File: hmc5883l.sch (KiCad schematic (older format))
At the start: 6 parts, among them U5 HMC5883L

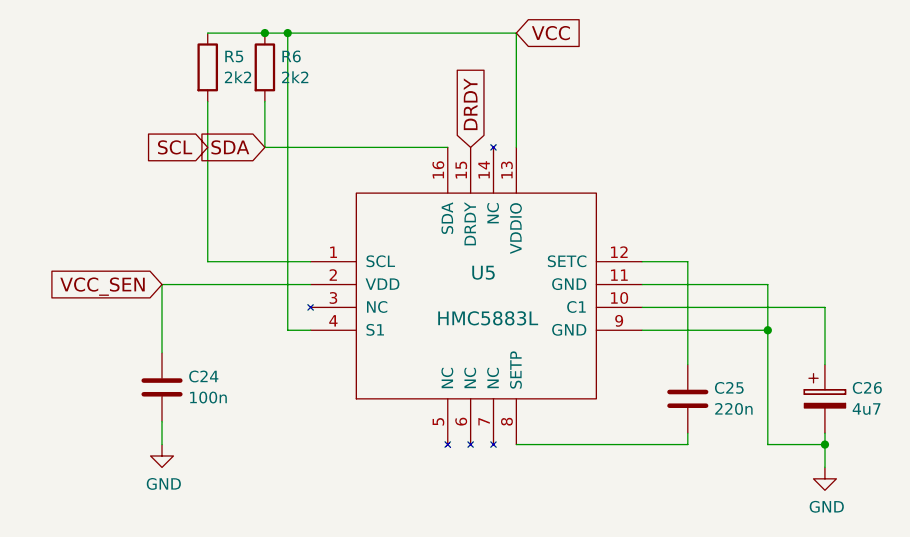
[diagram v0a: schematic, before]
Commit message: changed some netnames
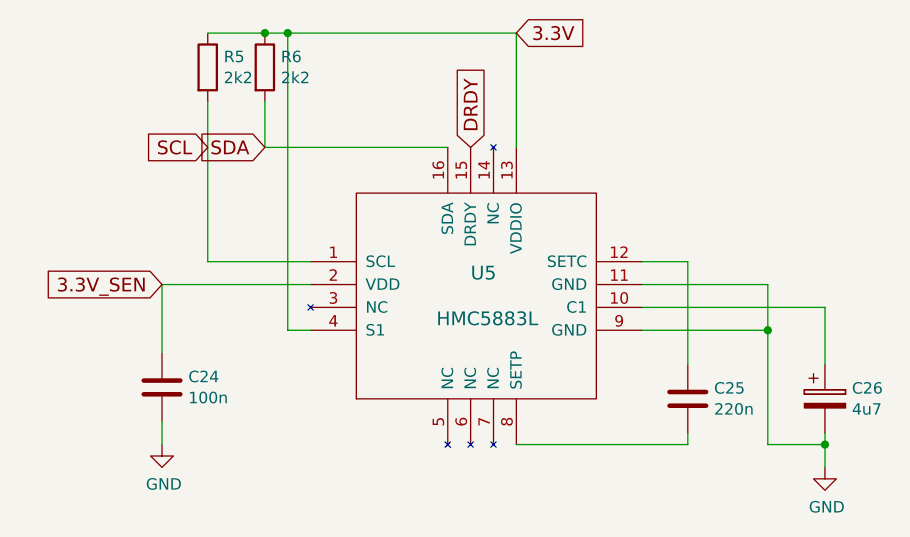
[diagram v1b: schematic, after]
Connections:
- net VCC renamed 3.3V
- net VCC_SEN renamed 3.3V_SEN
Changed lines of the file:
@@
 DRDY
 Text GLabel 5900 2650 2    60   Input ~ 0
-VCC
+3.3V
 Text GLabel 4350 3750 0    60   Input ~ 0
-VCC_SEN
+3.3V_SEN
 Wire Wire Line
 	5900 2650 5900 3150
